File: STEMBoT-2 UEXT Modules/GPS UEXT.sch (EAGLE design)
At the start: 4 parts, among them U1 TESEO-LIV3F

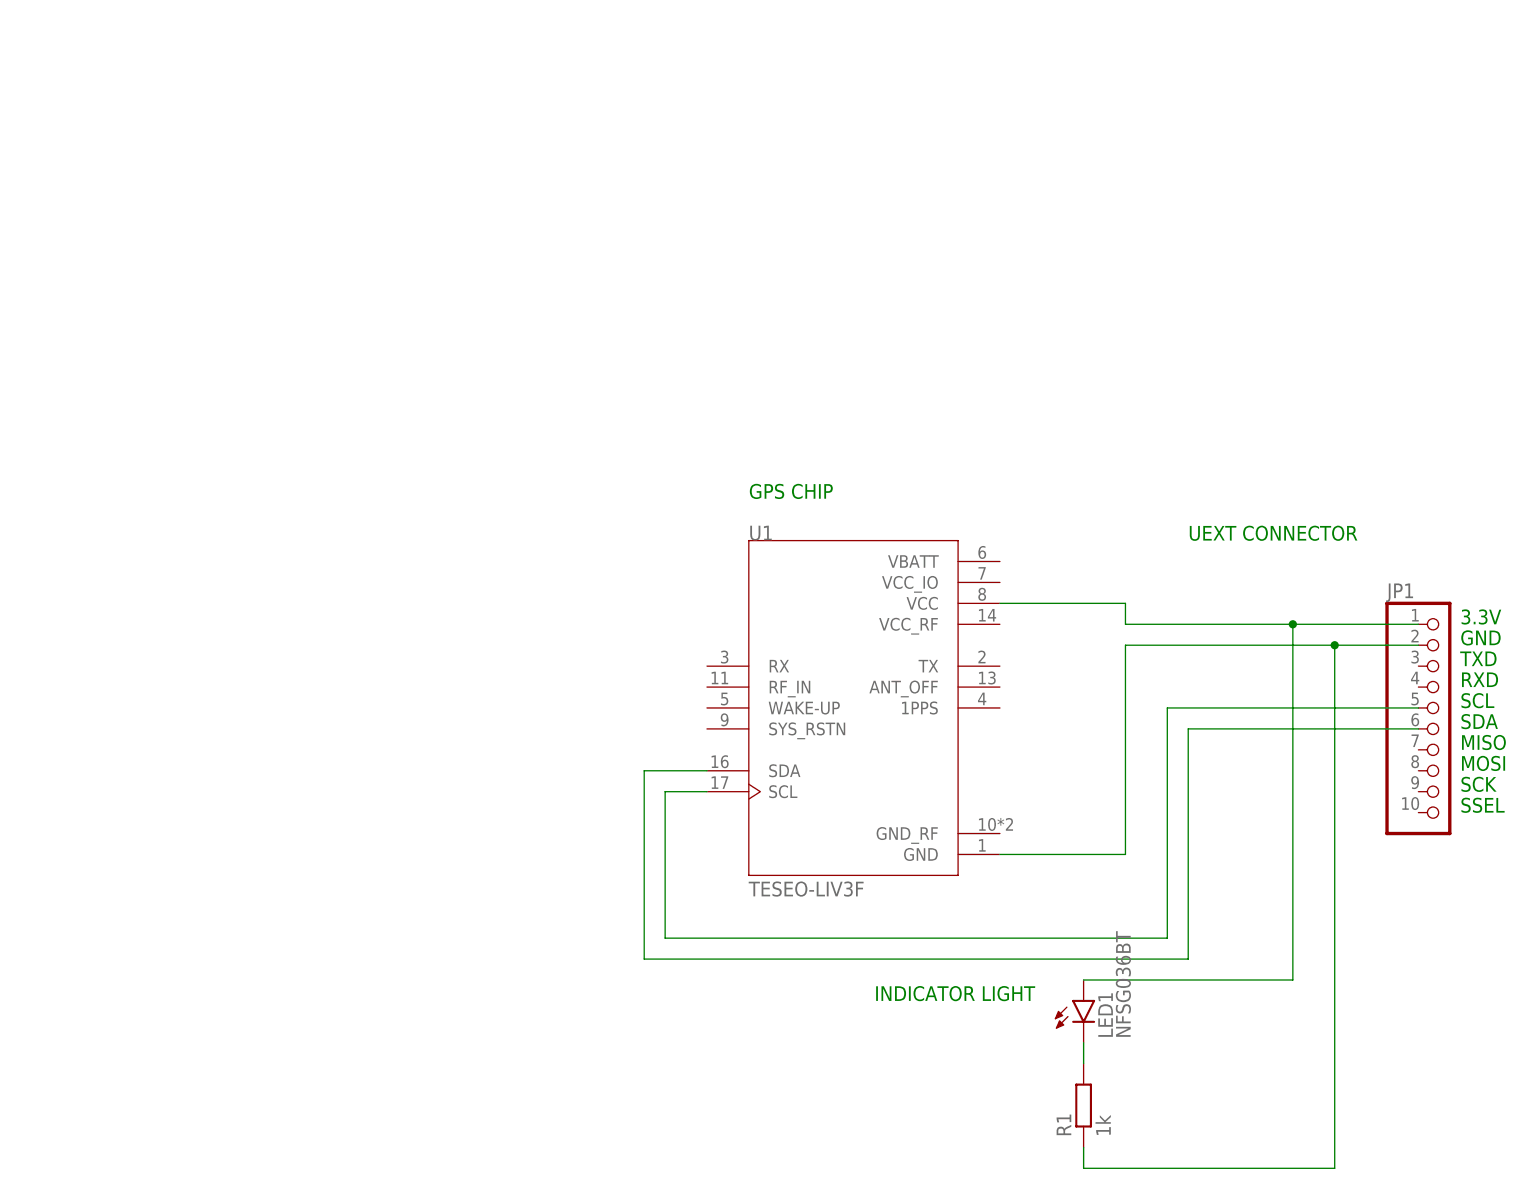
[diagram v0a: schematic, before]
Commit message: added new gps schematic and board
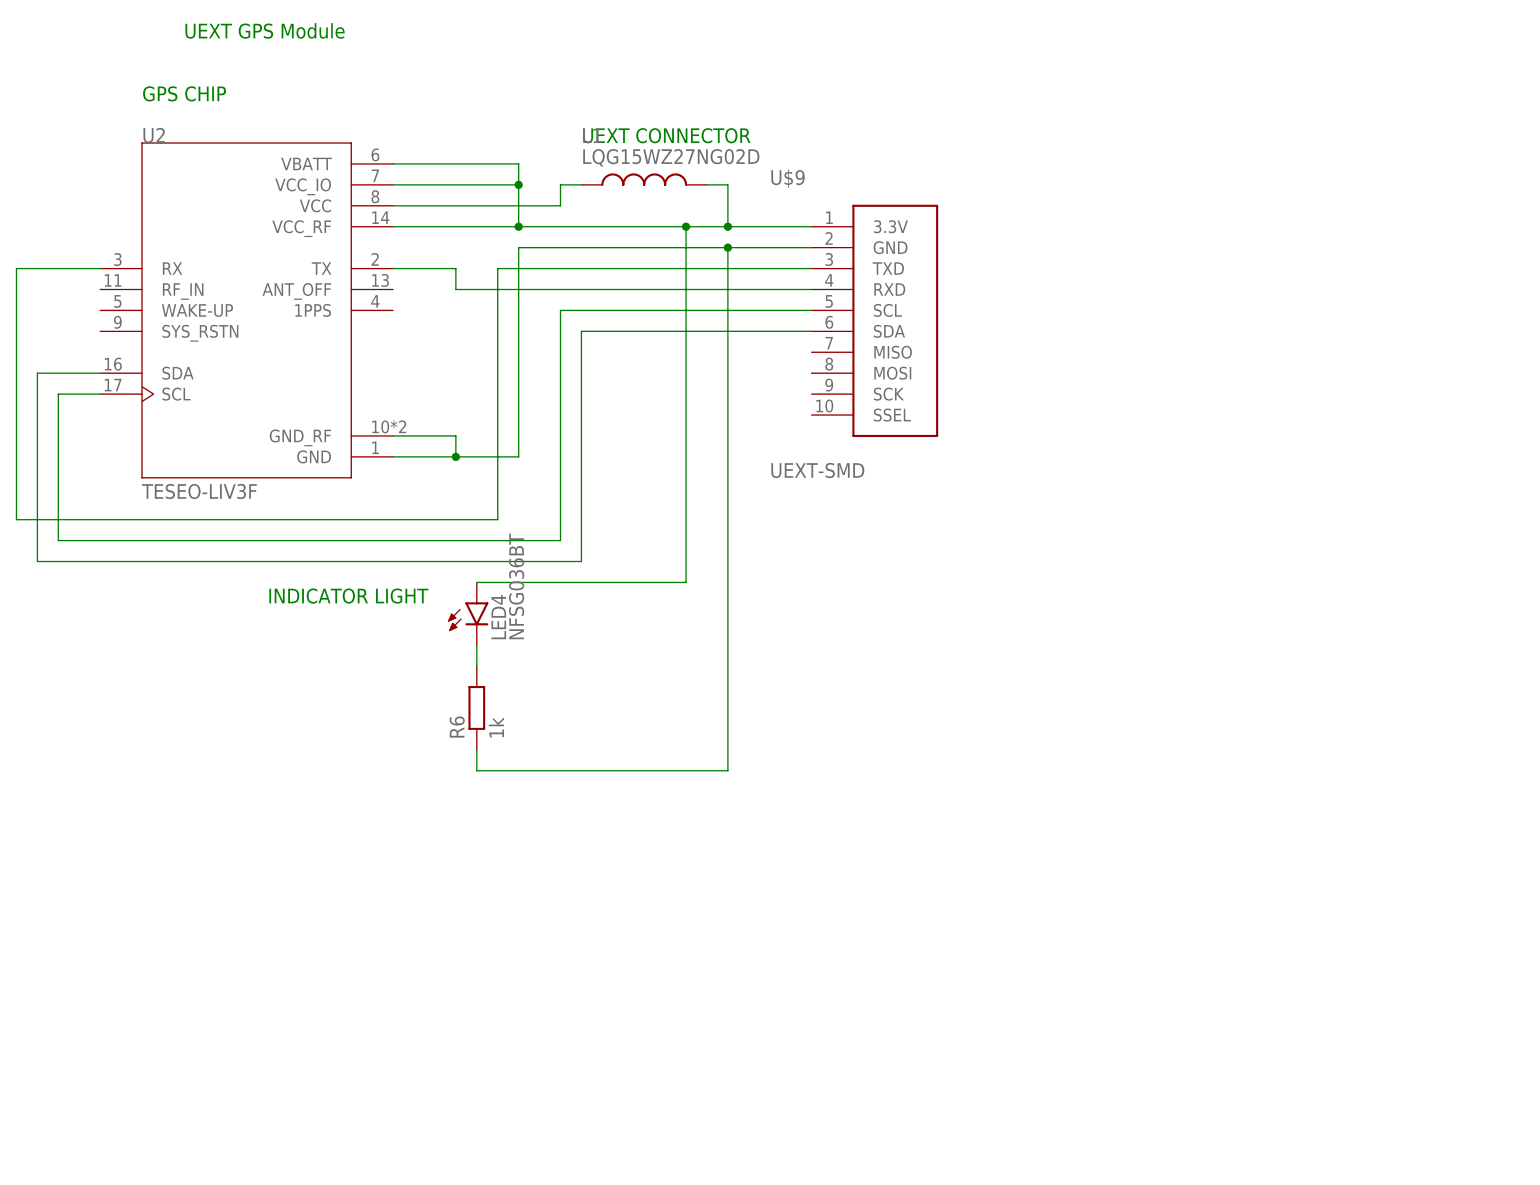
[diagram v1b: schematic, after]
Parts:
- removed JP1: (no value), pinhead:PINHD-1X10/90
- removed LED1: NFSG036BT, led:NFSG036BT
- removed R1: 1k, rcl:R-EU_M1206
- removed U1: TESEO-LIV3F, TESEO-LIV3F:TESEO-LIV3F
- added L1: LQG15WZ27NG02D, LQG15WZ27NG02D:LQG15WZ27NG02D
- added LED4: NFSG036BT, led:NFSG036BT
- added R6: 1k, rcl:R-EU_M1206
- added U$9: UEXT-SMD, UEXT-Connecotr:UEXT-SMD
- added U2: TESEO-LIV3F, TESEO-LIV3F:TESEO-LIV3F
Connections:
- removed net N$4: JP1.6, U1.SDA
- removed net N$5: LED1.C, R1.2
- new net N$21: R6.1, U$9.GND, U2.GND, U2.GND_RF
- new net N$22: L1.2, LED4.A, U$9.3.3V, U2.VBATT, U2.VCC_IO, U2.VCC_RF
- new net N$23: U$9.SCL, U2.SCL
- new net N$24: U$9.SDA, U2.SDA
- new net N$25: LED4.C, R6.2
- net N$1: now also U$9.RXD, U2.TX; no longer JP1.2, R1.1, U1.GND
- net N$2: now also U$9.TXD, U2.RX; no longer JP1.1, LED1.A, U1.VCC
- net N$3: now also L1.1, U2.VCC; no longer JP1.5, U1.SCL
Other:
- note added: "UEXT GPS Module"
- note removed: "3.3V"
- note removed: "GND"
- note removed: "MISO"
- note removed: "MOSI"
- note removed: "RXD"
- note removed: "SCK"
- note removed: "SCL"
- note removed: "SDA"
- note removed: "SSEL"
- note removed: "TXD"
